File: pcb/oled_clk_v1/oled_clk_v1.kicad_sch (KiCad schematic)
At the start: 8 parts, among them J1 Conn_01x15, J2 Conn_01x04, U1 MCP2210x-SO, Y1 Crystal

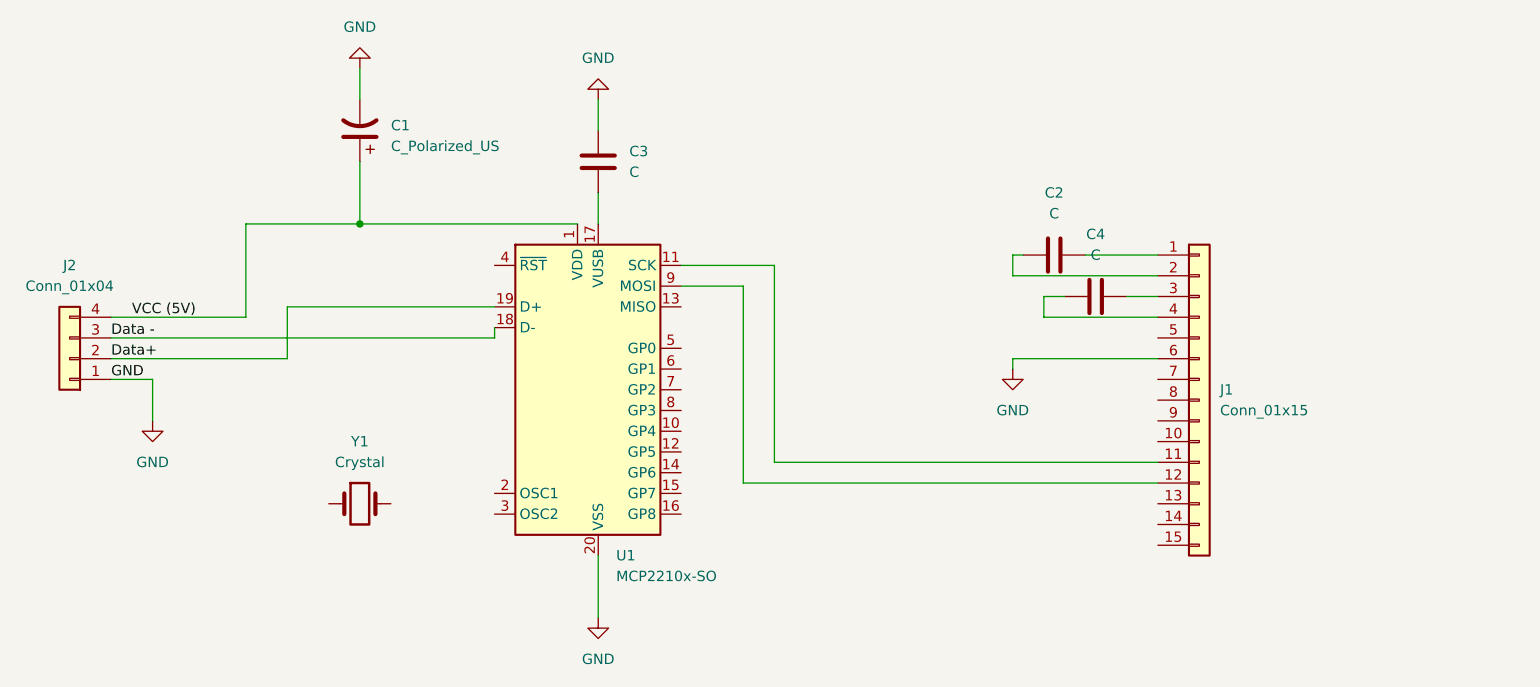
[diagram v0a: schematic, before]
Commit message: Updated schematic with connections - Connected oscillator to IC - Connected some voltage signals to OLED Connector
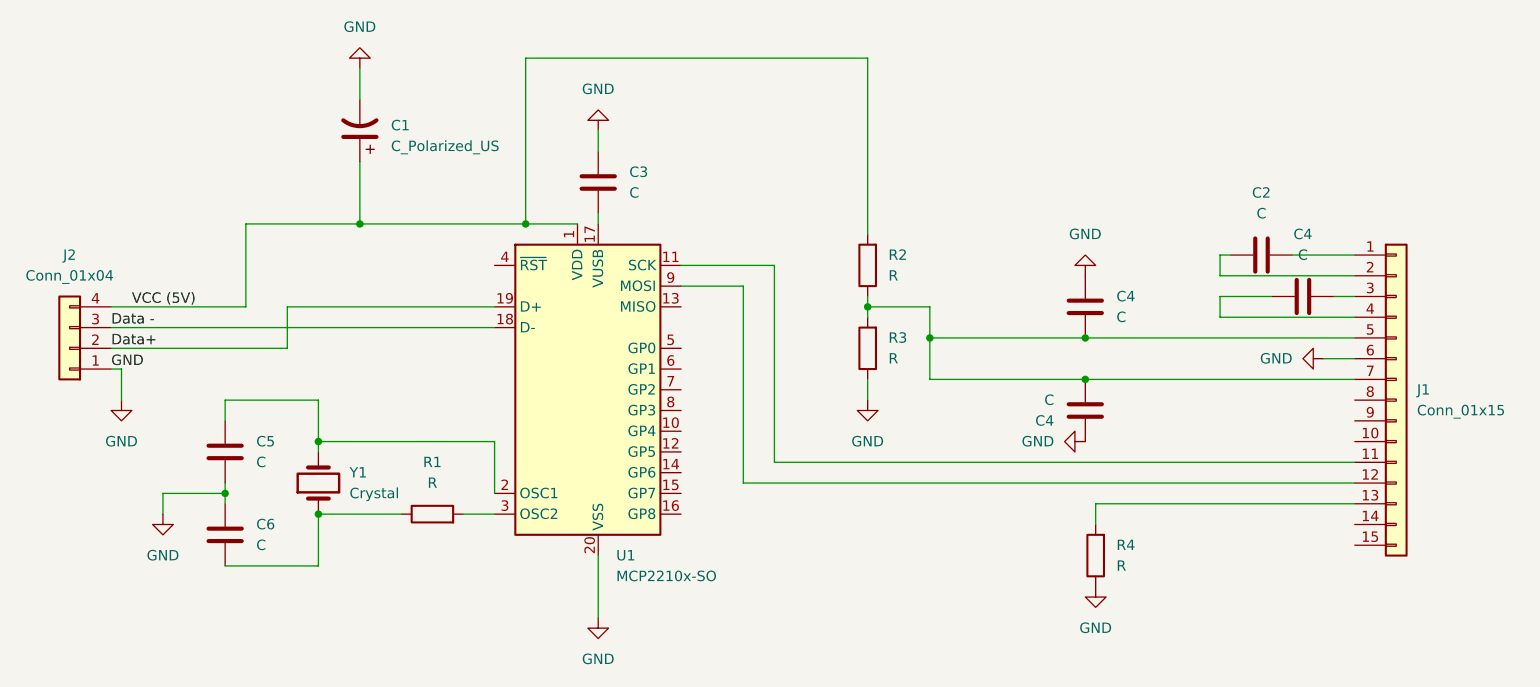
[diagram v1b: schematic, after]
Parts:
- added C4 (x2), C5, C6: C, symbol Device:C
- added R1, R2, R3, R4: R, symbol Device:R
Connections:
- net GND: now also C4.1, C4.1, C5.2, C6.1, R3.1, R4.1
- net VCC (5V): now also R2.2
- net at U1.2 (OSC1): now also Y1.2, C5.1
- net at U1.3 (OSC2): now also R1.2
- net at J1.13 (Pin_13): now also R4.2
- net at J1.5 (Pin_5): now also J1.7 (Pin_7), C4.2, C4.2, R2.1, R3.2
- net at Y1.1: now also C6.2, R1.1
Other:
- moved on the sheet: C2, C3, C4, J1, J2, Y1

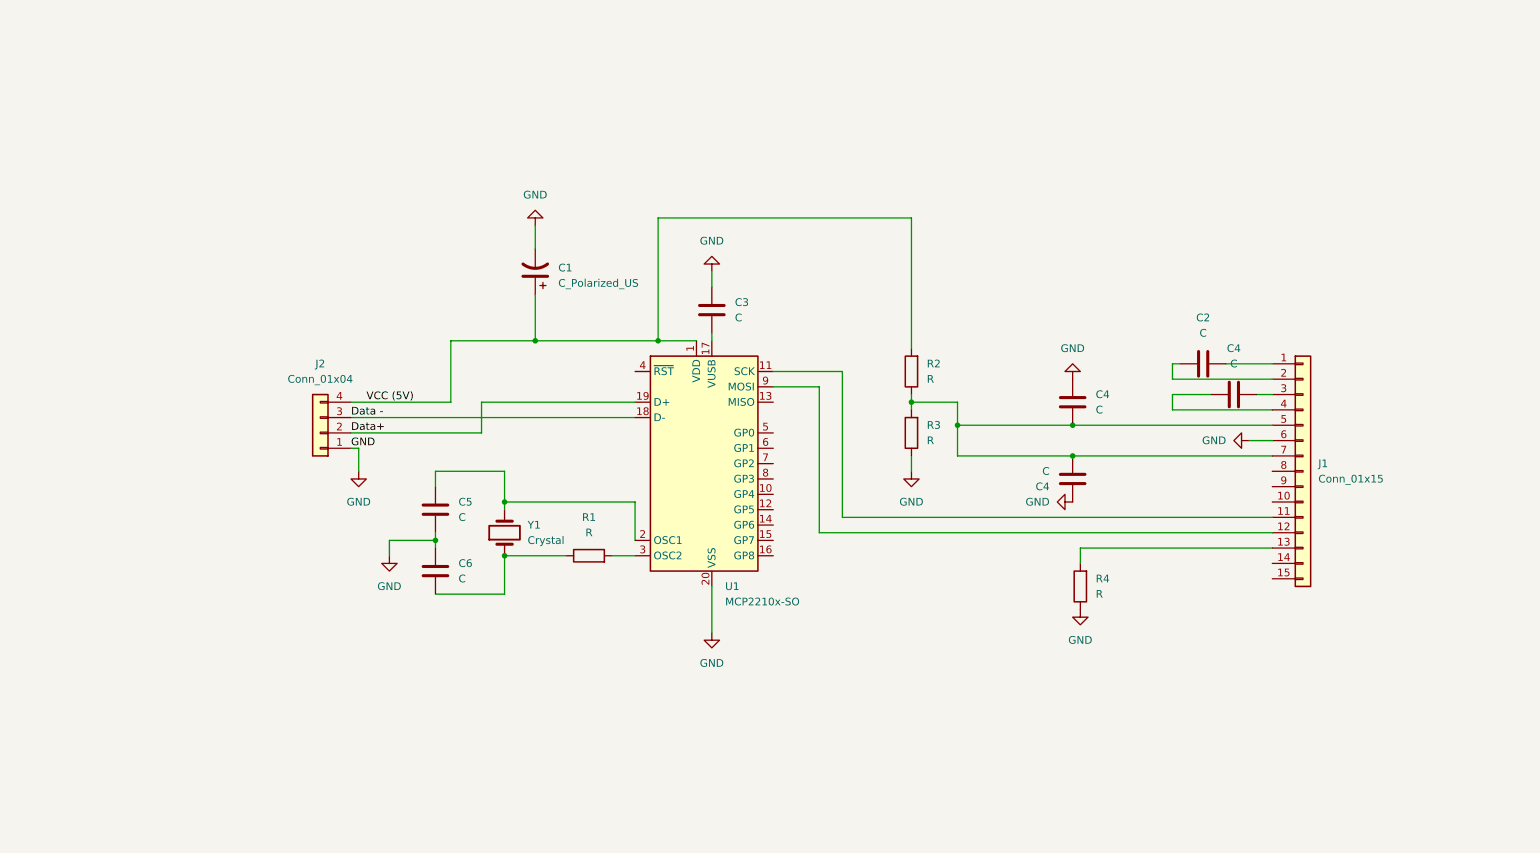
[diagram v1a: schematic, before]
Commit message: Added Labels and completed connections. - This commit include a significant number of changes to the schematic. All of   the direct connections have been removed in favor of labels, which greatly   abstracts away the complexity of the design. - connected all of the necessary signals together. - Updated design to used an LDO to drop the 5V power supply into 3.3V. - set up entire schematic to use 3.3V
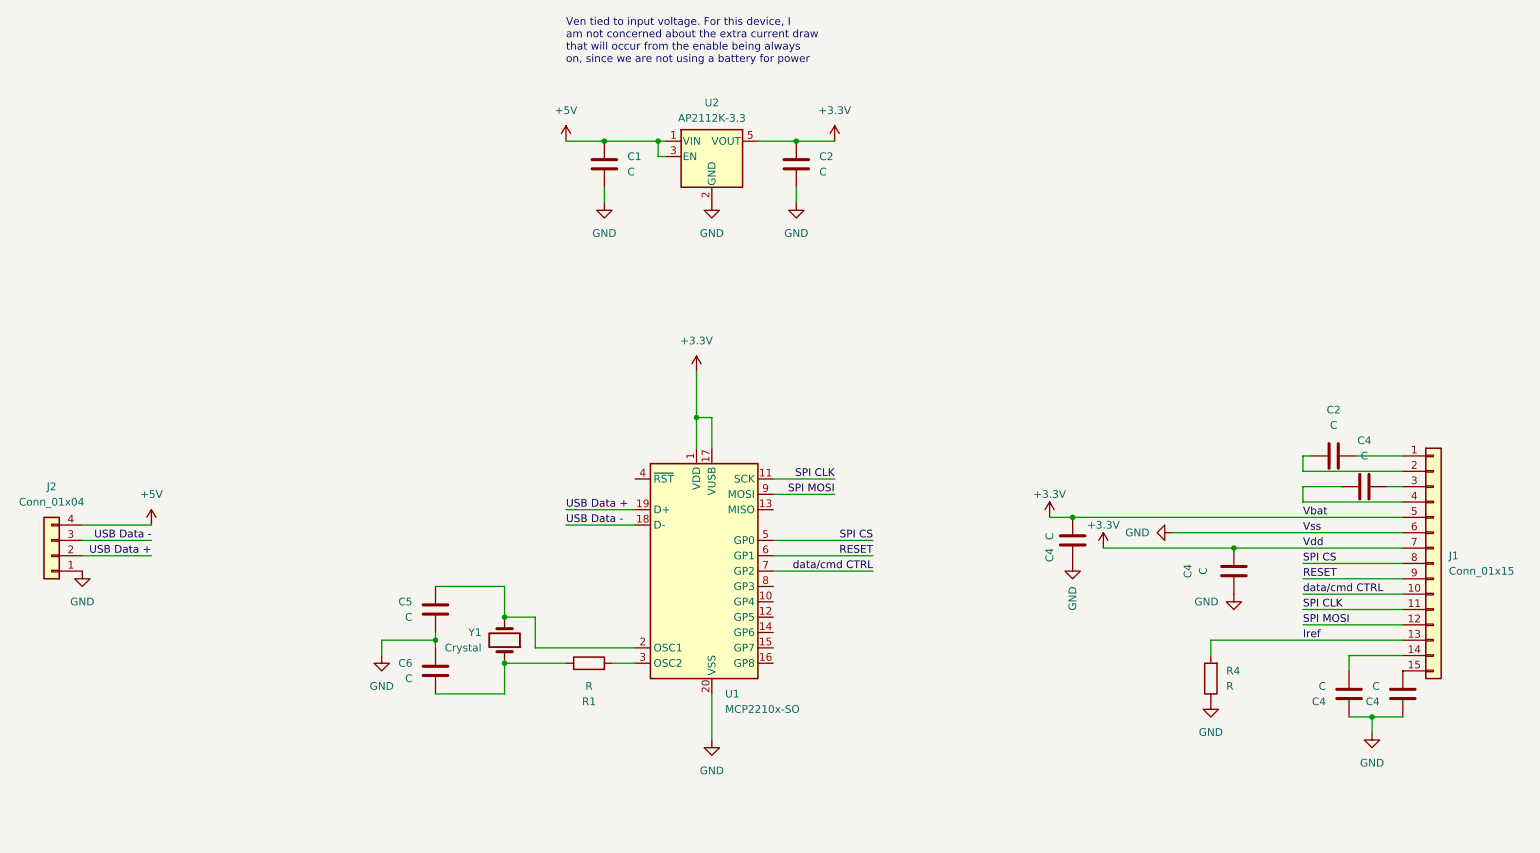
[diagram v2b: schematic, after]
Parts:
- removed C1: C_Polarized_US, symbol Device:C_Polarized_US
- removed C3: C, symbol Device:C
- removed R2, R3: R, symbol Device:R
- added C1, C2, C4 (x2): C, symbol Device:C
- added U2: AP2112K-3.3, Package_TO_SOT_SMD:SOT-23-5, symbol Regulator_Linear:AP2112K-3.3
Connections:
- net GND: now also C1.2, C2.2, C4.1, C4.1, U2.2 (GND)
- net +3.3V: now reaches C4.2, C4.2, J1.5 (Pin_5), J1.7 (Pin_7)
- net +3.3V: now also U1.1 (VDD), U1.17 (VUSB), C2.1, U2.5 (VOUT)
- net Iref: now reaches J1.13 (Pin_13), R4.2
- net SPI CLK: now reaches J1.11 (Pin_11), U1.11 (SCK)
- net SPI CS: now reaches U1.5 (GP0)
- net SPI CS: now also J1.8 (Pin_8)
- net RESET: now reaches U1.6 (GP1)
- net RESET: now also J1.9 (Pin_9)
- net data/cmd CTRL: now reaches U1.7 (GP2)
- net data/cmd CTRL: now also J1.10 (Pin_10)
- net SPI MOSI: now reaches J1.12 (Pin_12), U1.9 (MOSI)
- net at J1.14 (Pin_14): now also C4.2
- net at J1.15 (Pin_15): now also C4.2
- net Data - renamed USB Data -
- net Data+ renamed USB Data +
- net VCC (5V) renamed +5V
- net +5V: now also C1.1, U2.1 (VIN), U2.3 (EN); no longer U1.1 (VDD)
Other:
- note added: "Ven tied to input voltage. For this device, I am not concerned about the extra current draw that will occur from the enable being always on, since we are not using a battery for power"
- moved on the sheet: C2, C4, C5, C6, J1, J2, R1, R4, U1, Y1

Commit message: Re-designed schematic for a different display.
This display has a different number of pins for connectors, and has different
voltage requirements, so a number of changes needed to be made
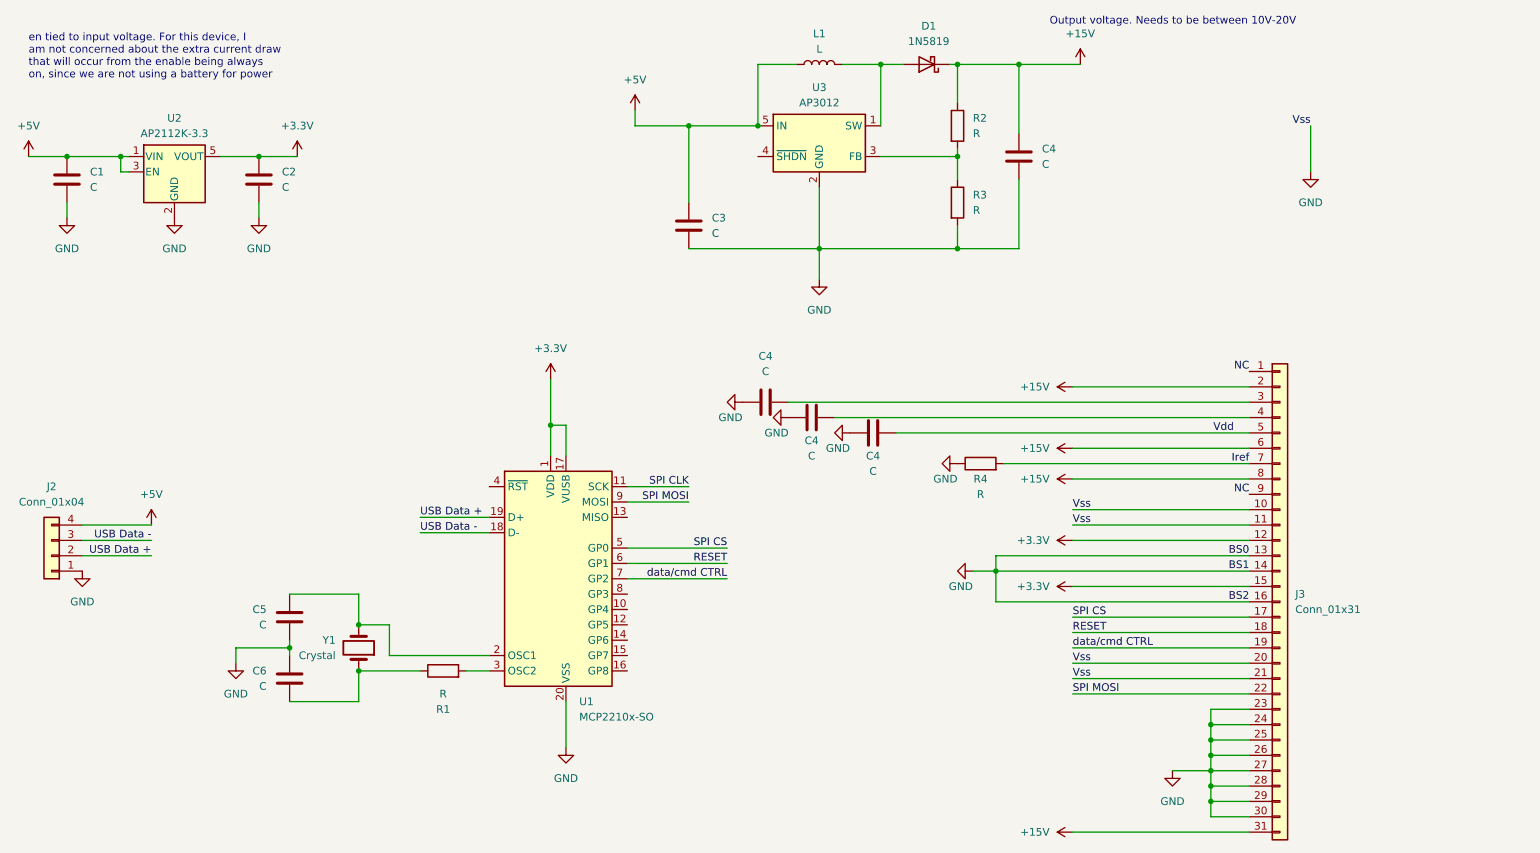
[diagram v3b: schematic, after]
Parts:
- removed C2, C4 (x5): C, symbol Device:C
- removed J1: Conn_01x15, symbol Connector_Generic:Conn_01x15
- added C3, C4 (x4): C, symbol Device:C
- added D1: 1N5819, Diode_THT:D_DO-41_SOD81_P10.16mm_Horizontal, symbol Diode:1N5819
- added J3: Conn_01x31, symbol Connector_Generic:Conn_01x31
- added L1: L, symbol Device:L
- added R2, R3: R, symbol Device:R
- added U3: AP3012, Package_TO_SOT_SMD:SOT-23-5, symbol Regulator_Switching:AP3012
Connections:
- net +3.3V: now also J3.12 (Pin_12), J3.15 (Pin_15)
- net +5V: now also C3.1, L1.1, U3.5 (IN)
- net GND: now also C3.2, C4.2, C4.2, C4.2, C4.2, J3.10 (Pin_10), J3.11 (Pin_11), J3.13 (Pin_13), J3.14 (Pin_14), J3.16 (Pin_16), J3.20 (Pin_20), J3.21 (Pin_21), J3.23 (Pin_23), J3.24 (Pin_24), J3.25 (Pin_25), J3.26 (Pin_26), J3.27 (Pin_27), J3.28 (Pin_28), J3.29 (Pin_29), J3.30 (Pin_30), R3.2, U3.2 (GND)
- net Iref: now also J3.7 (Pin_7)
- net RESET: now also J3.18 (Pin_18)
- net SPI CS: now also J3.17 (Pin_17)
- net SPI MOSI: now also J3.22 (Pin_22)
- net data/cmd CTRL: now also J3.19 (Pin_19)
- new net: C4.1, J3.3 (Pin_3)
- new net: C4.1, J3.4 (Pin_4)
- new net: R2.2, R3.1, U3.3 (FB)
- new net: D1.2 (A), L1.2, U3.1 (SW)
- new net +15V: C4.1, D1.1 (K), J3.2 (Pin_2), J3.31 (Pin_31), J3.6 (Pin_6), J3.8 (Pin_8), R2.1
- new net NC: J3.1 (Pin_1), J3.9 (Pin_9)
- new net Vdd: C4.1, J3.5 (Pin_5)
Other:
- note added: "Output voltage. Needs to be between 10V-20V"
- note added: "en tied to input voltage. For this device, I am not concerned about the extra current draw that will occur from the enable being always on, since we are not using a battery for power"
- note removed: "Ven tied to input voltage. For this device, I am not concerned about the extra current draw that will occur from the enable being always on, since we are not using a battery for power"
- moved on the sheet: C1, C2, C5, C6, R1, U1, U2, Y1
